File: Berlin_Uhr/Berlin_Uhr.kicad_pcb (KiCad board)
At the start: 2 copper layers, 100 x 130.1 mm, 53 parts, among them J1 USB_C_Receptacle_USB2.0, J2 ISP, Q1 KPS-3227, SW1 SW_Push, SW2 SW_Push, U1 DS3231M, U2 ATtiny167-SU, U3 TLC5947DAP, Y1 16MHz

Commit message: update PCB
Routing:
- net GND: track 361.9 -> 213.8 mm
- net Net-(BT1-Pad1): track 54.8 -> 56.1 mm
- net Net-(D15-Pad1): track 44.5 -> 45.3 mm
- net Net-(J2-Pad4): track 53.3 -> 52.8 mm
- net Net-(Q1-Pad2): track 106.5 -> 106.8 mm, vias 4 -> 3

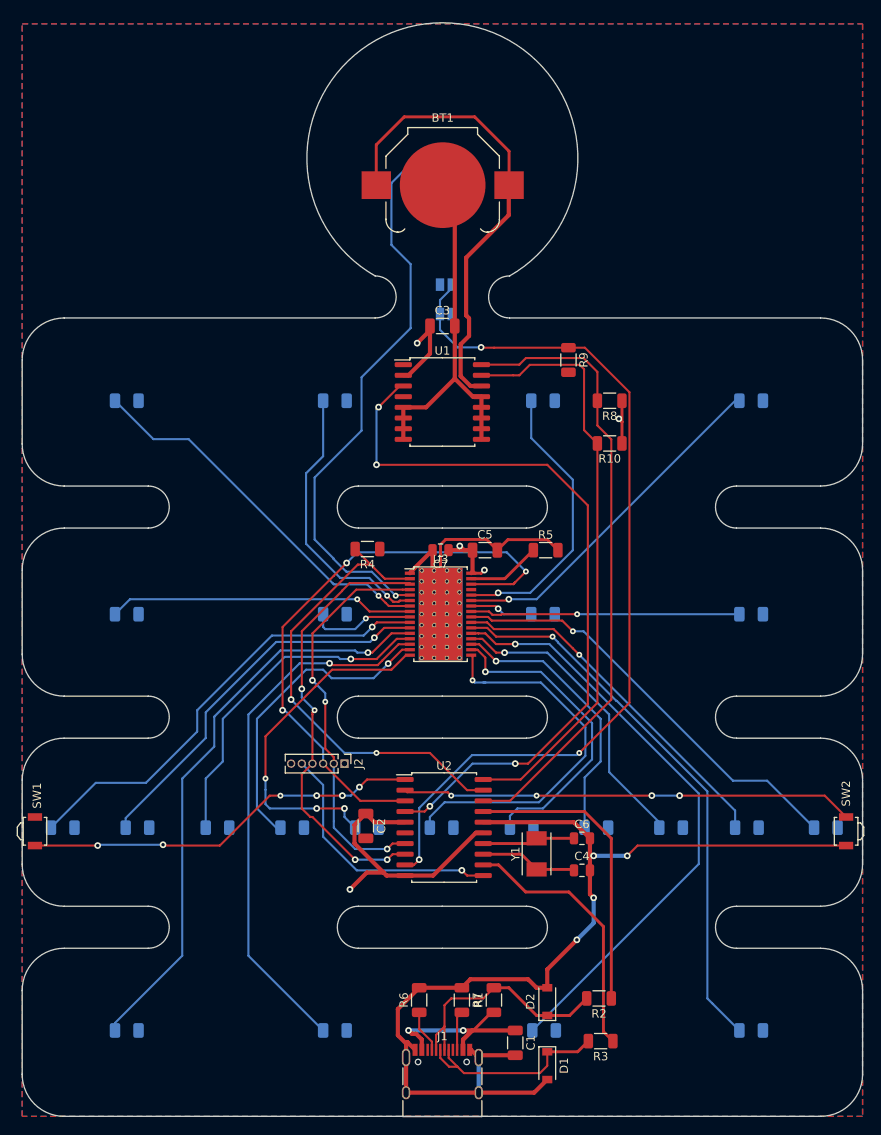
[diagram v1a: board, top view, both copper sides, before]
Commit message: Update PCB
improved layout
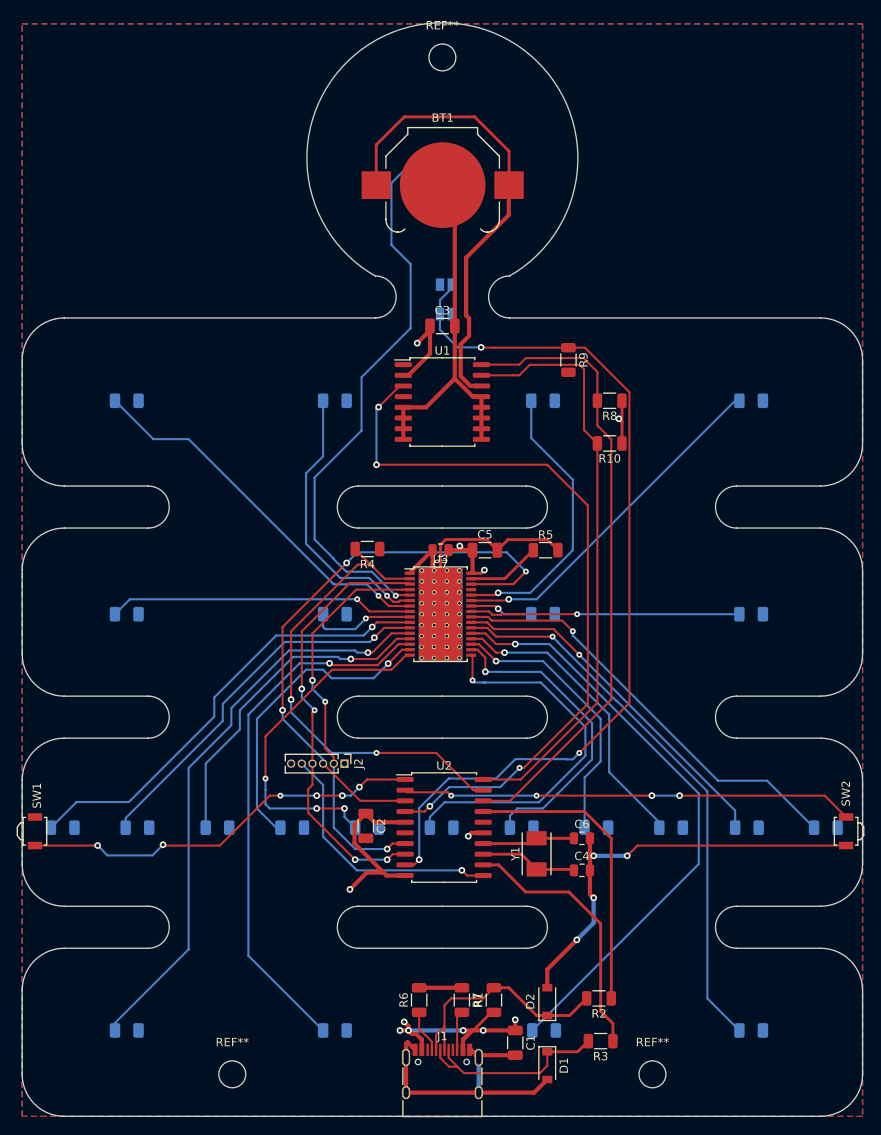
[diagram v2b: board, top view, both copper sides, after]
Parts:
- added REF**: MountingHole_3.2mm_M3_DIN965, MountingHole:MountingHole_3.2mm_M3_DIN965, F.Cu at (170.0, 150.0)
- added REF**: MountingHole_3.2mm_M3_DIN965, MountingHole:MountingHole_3.2mm_M3_DIN965, F.Cu at (120.0, 150.0)
- added REF**: MountingHole_3.2mm_M3_DIN965, MountingHole:MountingHole_3.2mm_M3_DIN965, F.Cu at (145.0, 29.0)
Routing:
- net GND: track 213.8 -> 186.3 mm
- net +5V: track 82.9 -> 76.9 mm, vias 7 -> 12
- net Net-(SW1-Pad1): track 47.4 -> 48.3 mm
- net Net-(R4-Pad2): track 56.2 -> 57.1 mm
- net Net-(J2-Pad4): track 52.8 -> 52.0 mm
- net Net-(D9-Pad1): track 46.1 -> 45.5 mm
- net Net-(D11-Pad1): track 40.2 -> 39.6 mm
- net Net-(D10-Pad1): track 69.8 -> 69.2 mm

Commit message: Update PCB
USB track length symmetrical
LED tracks to 0,35mm
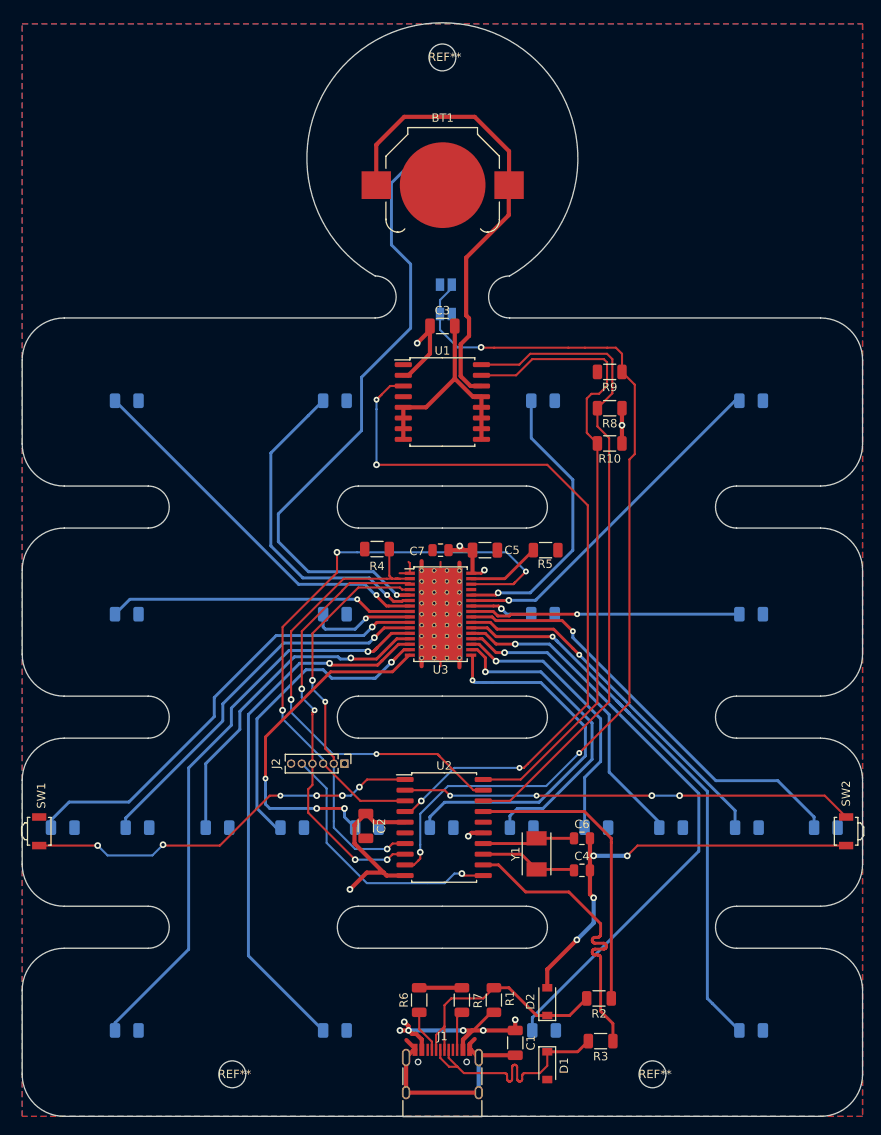
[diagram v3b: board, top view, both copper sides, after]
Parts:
- moved R9 5.11 mm to (164.9, 66.4), turned to 180 degrees
- moved R4 1.14 mm to (137.2, 87.5), turned to 0 degrees
- moved R8 0.89 mm to (164.9, 70.7)
- moved SW1 0.51 mm to (97.0, 121.1)
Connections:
- net Net-(D1-Pad1) renamed /D1+
- net Net-(D2-Pad1) renamed /D1-
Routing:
- net GND: track 186.3 -> 130.0 mm
- net Net-(D3-Pad1): track 68.2 -> 76.0 mm
- net Net-(D4-Pad1): track 33.1 -> 39.2 mm
- net /SDA: track 70.7 -> 75.8 mm
- net /D1+: track 24.3 -> 29.3 mm
- net /D+: track 31.4 -> 35.6 mm
- net /SCL: track 74.7 -> 78.3 mm
- net Net-(D20-Pad1): track 66.2 -> 68.6 mm
- net Net-(Q1-Pad2): track 106.9 -> 109.2 mm
- net Net-(J2-Pad3): track 71.1 -> 72.6 mm
- net Net-(U1-Pad3): track 89.1 -> 90.5 mm
- net Net-(J2-Pad5): track 30.7 -> 31.8 mm
- net +5V: track 76.9 -> 77.8 mm
- net Net-(D22-Pad1): track 51.5 -> 52.4 mm
- net Net-(D13-Pad1): track 36.8 -> 37.7 mm
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
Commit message: PCB with silkscreen
LED Side with grid
Component Side with Image
First Gerber Set
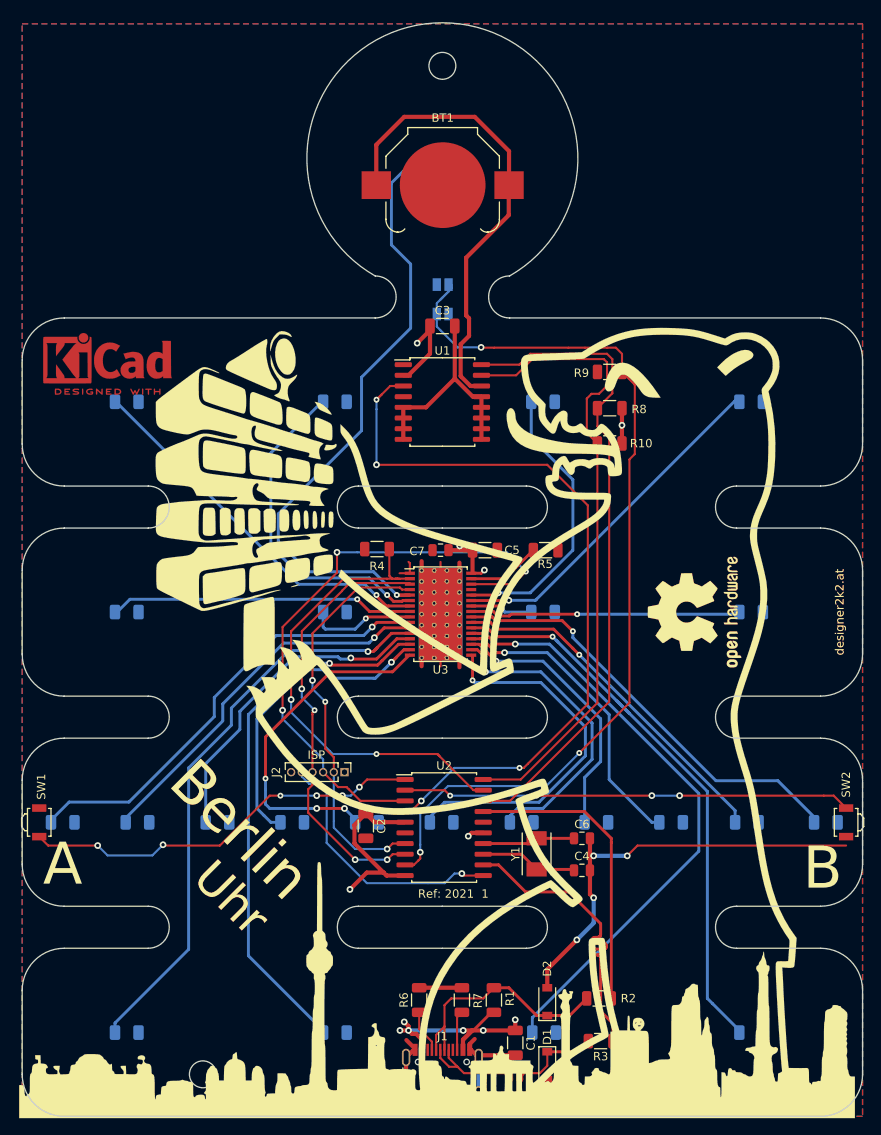
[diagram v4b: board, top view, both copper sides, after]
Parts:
- added G***: LOGO, Berlin_Uhr:Berlin-Uhr-Front, F.Cu at (145.0, 90.0)
- added G***: LOGO, Berlin_Uhr:LED-Frame, B.Cu at (145.0, 90.0)
- added REF**: OSHW-Logo2_14.6x12mm_SilkScreen, Symbol:OSHW-Logo2_14.6x12mm_SilkScreen, F.Cu at (175.0, 95.0)
- added REF**: OSHW-Logo2_14.6x12mm_Copper, Symbol:OSHW-Logo2_14.6x12mm_Copper, F.Cu at (175.0, 95.0)
- added REF**: KiCad-Logo2_6mm_Copper, Symbol:KiCad-Logo2_6mm_Copper, F.Cu at (105.2, 64.8)
- moved REF** 3.50 mm to (173.5, 150.0)
- moved REF** 3.50 mm to (116.5, 150.0)
- moved SW1 1.06 mm to (97.0, 120.0)
- moved SW2 1.06 mm to (193.0, 120.0)
- moved J2 1.02 mm to (133.3, 114.0)
- moved REF** 1.00 mm to (145.0, 30.0)
- moved D11 0.64 mm to (118.2, 120.0)
- moved D13 0.64 mm to (127.1, 120.0)
- moved D14 0.64 mm to (136.0, 120.0)
- moved D15 0.64 mm to (144.9, 120.0)
- moved D16 0.64 mm to (154.4, 120.0)
- moved D17 0.64 mm to (163.3, 120.0)
- moved D18 0.64 mm to (172.2, 120.0)
- moved D21 0.64 mm to (181.2, 120.0)
- moved D22 0.64 mm to (190.6, 120.0)
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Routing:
- net Net-(Q1-Pad2): track 109.2 -> 112.2 mm
- net Net-(D14-Pad1): track 41.6 -> 41.0 mm
- net Net-(J2-Pad3): track 72.6 -> 73.2 mm
- net Net-(D18-Pad1): track 36.1 -> 36.6 mm
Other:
- board text added: "A"
- board text added: "B"
- board text added: "Berlin"
- board text added: "ISP"
- board text added: "Ref: 2021 1"
- board text added: "Uhr"
- board text added: "designer2k2.at"

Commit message: PCB Update (getting close)
this is getting close to be ordered
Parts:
- added BerlinUhr: G***, Berlin_Uhr:BerlinUhrLogo, F.Cu at (108.0, 114.0)
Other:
- board text removed: "Berlin"
- board text removed: "Uhr"

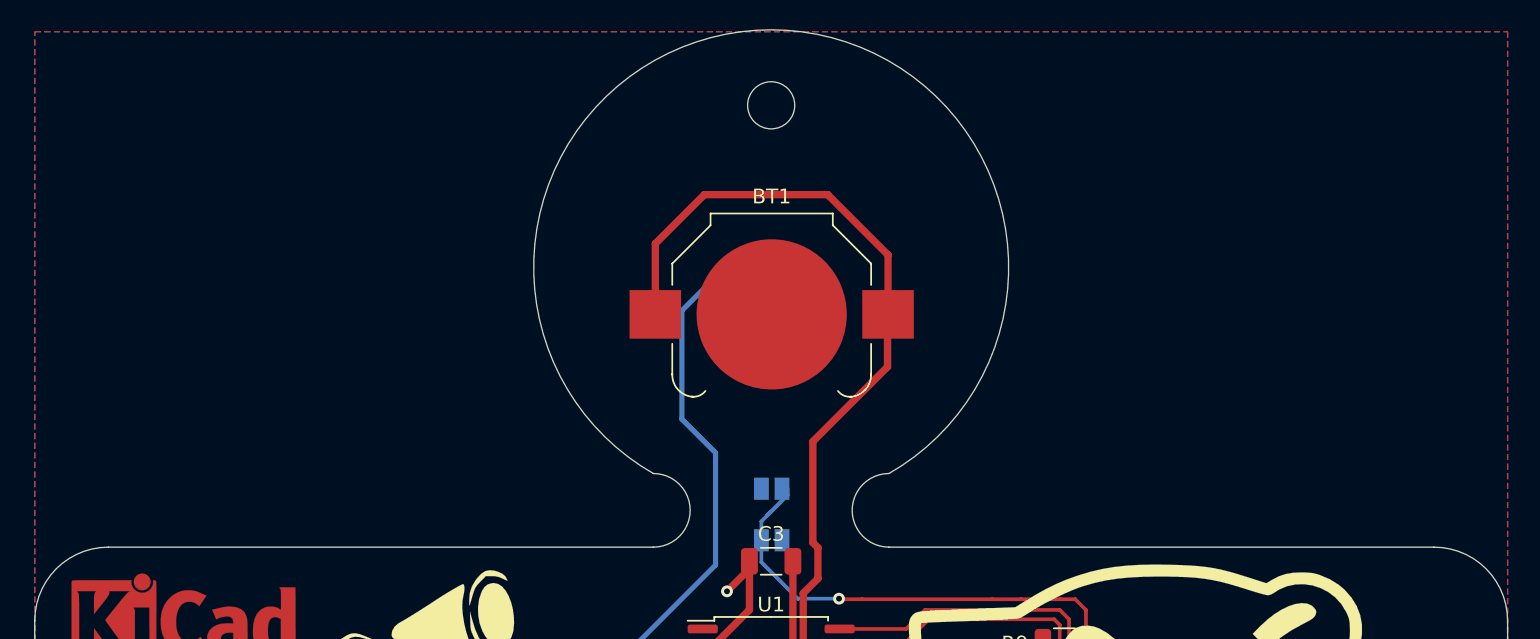
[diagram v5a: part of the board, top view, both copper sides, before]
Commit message: add breakaway tabs for documentation
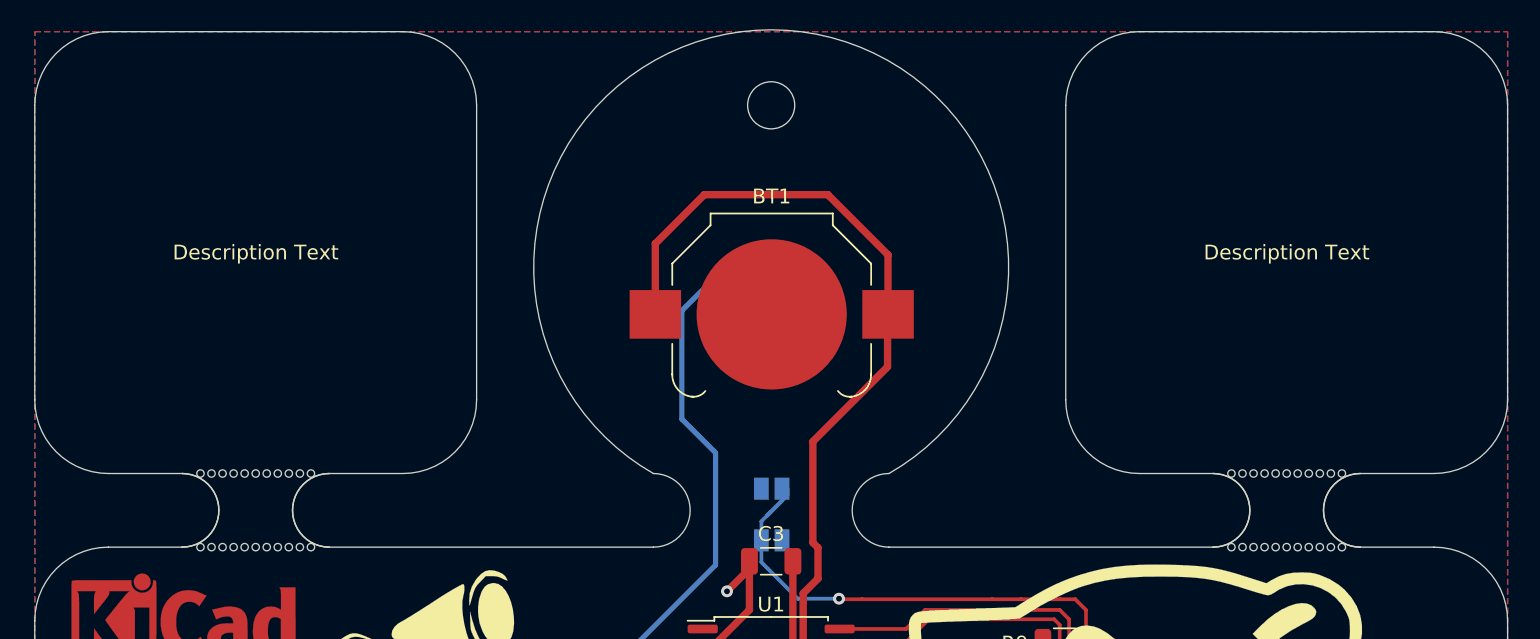
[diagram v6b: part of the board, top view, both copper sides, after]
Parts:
- added mouse-bite-5mm-slot: VAL**, Berlin_Uhr:mouse-bite-5mm-slot, F.Cu at (110.0, 57.5)
- added mouse-bite-5mm-slot: VAL**, Berlin_Uhr:mouse-bite-5mm-slot, F.Cu at (180.0, 57.5)
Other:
- outline, holes or cut-outs redrawn
- board text added: "Description Text"

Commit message: PCB to order
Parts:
- removed mouse-bite-5mm-slot (x2): VAL**, Berlin_Uhr:mouse-bite-5mm-slot
- moved R9 22.3 mm to (171.7, 87.6), turned to 0 degrees
- moved R10 17.3 mm to (166.1, 92.2)
- moved R8 16.9 mm to (166.1, 87.6)
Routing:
- net /SDA: track 75.8 -> 65.7 mm
- net /SCL: track 78.3 -> 69.5 mm
- net +5V: track 77.8 -> 75.7 mm
- net Net-(Q1-Pad2): track 112.2 -> 110.0 mm
- net Net-(U1-Pad3): track 90.5 -> 91.4 mm
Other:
- outline, holes or cut-outs redrawn
- board text removed: "Description Text"

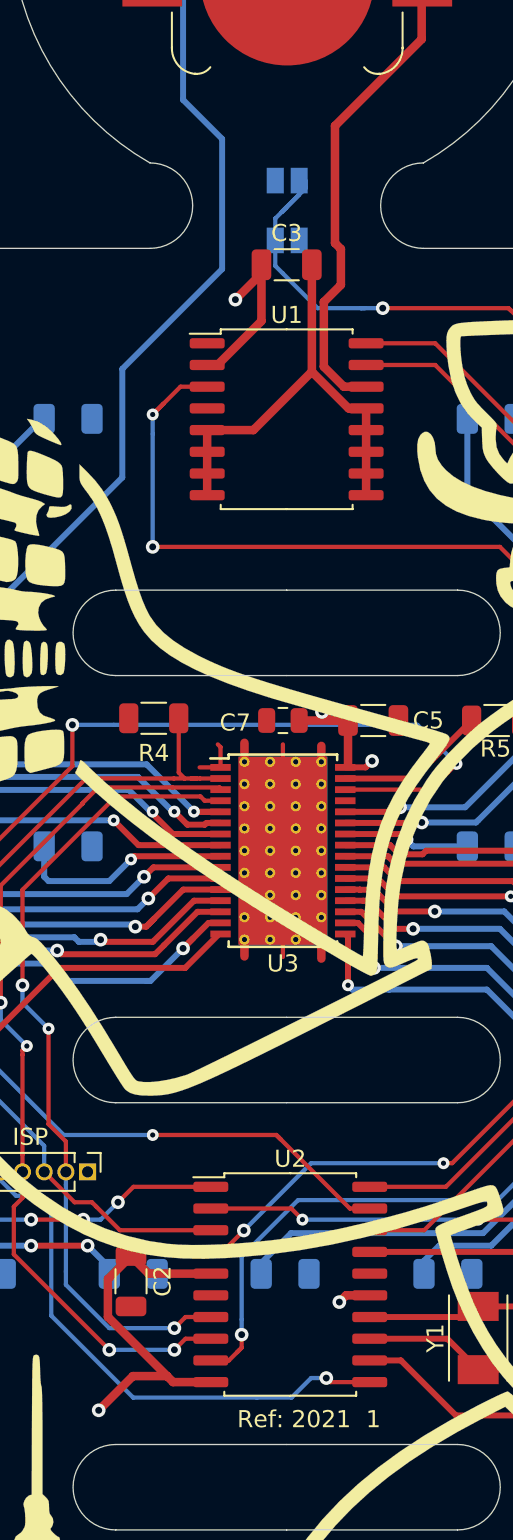
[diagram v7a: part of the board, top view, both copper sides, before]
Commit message: PCB Update / Bugfix after first Batch
- R4 now a pullup for Blank, not pulldown
- add text that the battery is a  CR1216
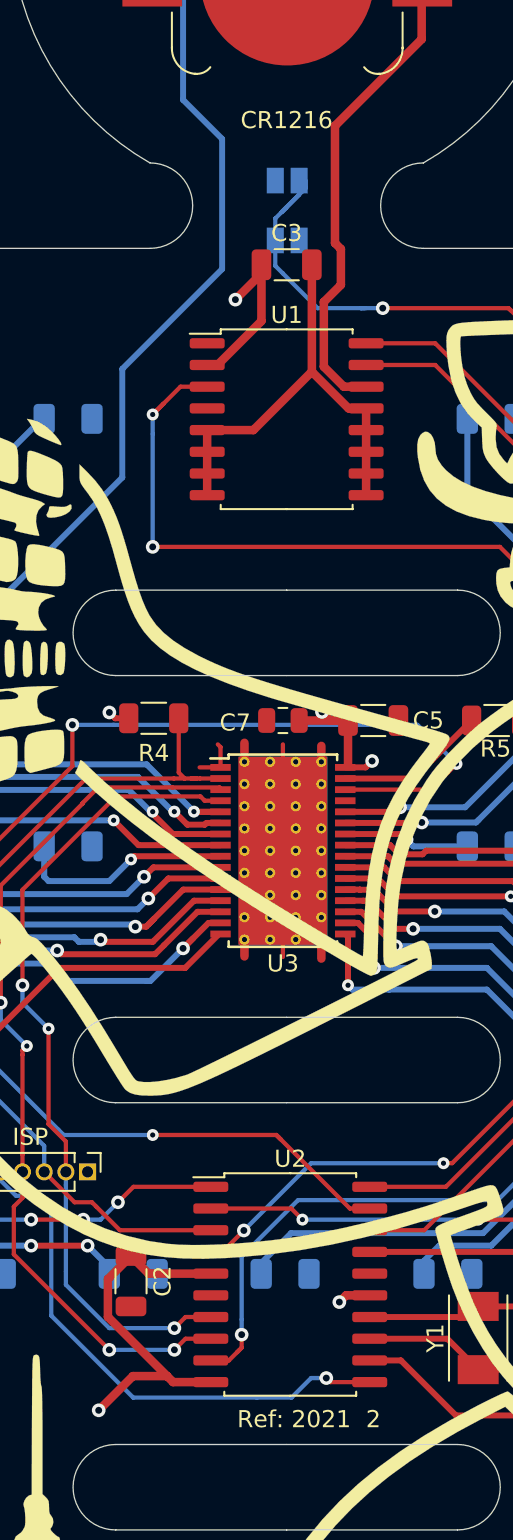
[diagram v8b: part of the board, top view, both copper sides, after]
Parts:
- BT1: value Battery -> CR1216
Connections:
- R4 pad 1: GND -> +5V
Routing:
- net +5V: track 75.7 -> 76.9 mm, vias 12 -> 13
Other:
- board text added: "CR1216"
- board text added: "Ref: 2021 2"
- board text removed: "Ref: 2021 1"
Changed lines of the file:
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@@
   (general
     (thickness 1.6)
-    (drawings 74)
-    (tracks 764)
+    (drawings 75)
+    (tracks 767)
     (zones 0)
     (modules 62)
@@
       (net 41 "Net-(R4-Pad2)"))
     (pad 1 smd roundrect (at -1.4625 0) (size 1.125 1.75) (layers F.Cu F.Paste F.Mask) (roundrect_rratio 0.2222195555555556)
-      (net 1 GND))
+      (net 3 +5V))
     (model ${KISYS3DMOD}/Resistor_SMD.3dshapes/R_1206_3216Metric.wrl
       (at (xyz 0 0 0))
@@
       (effects (font (size 1 1) (thickness 0.15)))
     )
-    (fp_text value Battery (at 0 7.5) (layer F.Fab)
+    (fp_text value CR1216 (at 0 7.5) (layer F.Fab)
       (effects (font (size 1 1) (thickness 0.15)))
     )
@@
     )
   )
+  (gr_text CR1216 (at 145 52.5) (layer F.SilkS)
+    (effects (font (size 1 1) (thickness 0.15)))
+  )
   (gr_line (start 137 60) (end 105 60) (layer Edge.Cuts) (width 0.05))
   (gr_line (start 190 60) (end 175 60) (layer Edge.Cuts) (width 0.05))
@@
     (effects (font (size 3 3) (thickness 0.5)))
   )
-  (gr_text "Ref: 2021  1" (at 146.304 128.524) (layer F.SilkS)
+  (gr_text "Ref: 2021  2" (at 146.304 128.524) (layer F.SilkS)
     (effects (font (size 1 1) (thickness 0.15)))
   )
@@
   (segment (start 134.53999 122.534956) (end 134.53999 120.32001) (width 0.5) (layer F.Cu) (net 3))
   (segment (start 140.56 126.35) (end 138.355034 126.35) (width 0.5) (layer F.Cu) (net 3))
-  (segment (start 145.73 87.63) (end 148.59 87.63) (width 0.5) (layer F.Cu) (net 3))
   (segment (start 148.59 87.63) (end 148.59 90.215) (width 0.5) (layer F.Cu) (net 3))
   (segment (start 140.953544 66.825) (end 140.35 66.825) (width 0.5) (layer F.Cu) (net 3))
@@
   (segment (start 167.64 89.916) (end 167.64 92.202) (width 0.5) (layer F.Cu) (net 3))
   (via (at 167.64 89.916) (size 0.8) (drill 0.4) (layers F.Cu B.Cu) (net 3))
+  (via (at 134.624 87.159) (size 0.8) (drill 0.4) (layers F.Cu B.Cu) (net 3))
+  (segment (start 134.965 87.5) (end 134.624 87.159) (width 0.35) (layer F.Cu) (net 3))
+  (segment (start 135.759 87.5) (end 134.965 87.5) (width 0.35) (layer F.Cu) (net 3))
+  (segment (start 145.73 87.63) (end 148.59 87.63) (width 0.5) (layer F.Cu) (net 3))
   (segment (start 154.4 123.81) (end 156.21 125.62) (width 0.35) (layer F.Cu) (net 4))
   (segment (start 149.86 123.81) (end 154.4 123.81) (width 0.35) (layer F.Cu) (net 4))
